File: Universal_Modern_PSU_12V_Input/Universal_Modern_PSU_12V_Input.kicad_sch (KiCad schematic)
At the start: 24 parts, among them J1 +12VDC Input, J2 Power Output, Q1 SUP53P06-20-E3, U1 DFR0831, U2 NKE1212SC, U3 R-78CK5.0-0.5

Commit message: Thickened +5V & +12V tracks
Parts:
- C2: footprint Capacitor_THT:C_Radial_D6.3mm_H7.0mm_P2.50mm -> Capacitor_THT:CP_Radial_D6.3mm_P2.50mm
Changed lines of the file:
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@@
 		)
 	)
-	(text_box "Power Input\nUse a well-regulated 4-5A +12VDC power supply.\nExpects centre-postive polarity.\nMOSFET Q1 will block in case centre-negative is used.\nIf not required, bridge pins 2 (drain) and 3 (source)."
+	(text_box "Power Input\nUse a well-regulated ≥5A +12VDC power supply.\nExpects centre-postive polarity.\nMOSFET Q1 will block in case centre-negative is used.\nIf not required, bridge pins 2 (drain) and 3 (source)."
 		(exclude_from_sim no)
 		(at 25.4 50.8 0)
@@
 			)
 		)
-		(property "Footprint" "Capacitor_THT:C_Radial_D6.3mm_H7.0mm_P2.50mm"
+		(property "Footprint" "Capacitor_THT:CP_Radial_D6.3mm_P2.50mm"
 			(at 176.53 99.3648 0)
 			(effects

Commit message: Additional vias for heat conduction
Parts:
- C2: value 10µF -> 100µF; footprint Capacitor_THT:CP_Radial_D6.3mm_P2.50mm -> Capacitor_THT:CP_Radial_D8.0mm_P5.00mm
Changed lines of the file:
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@@
 			)
 		)
-		(property "Value" "10µF"
+		(property "Value" "100µF"
 			(at 177.546 98.806 90)
 			(effects
@@
 			)
 		)
-		(property "Footprint" "Capacitor_THT:CP_Radial_D6.3mm_P2.50mm"
+		(property "Footprint" "Capacitor_THT:CP_Radial_D8.0mm_P5.00mm"
 			(at 176.53 99.3648 0)
 			(effects

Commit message: Minor PCB & schematic changes
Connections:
- net +12V_{OUT} is gone; now on net +12V_{IN}: C2.1, C3.1, C6.1, C7.2, D1.2 (A), J2.2 (Pin_2), Q1.3 (S), TP2.1, U1.2 (IN+), U2.2 (+VIN), U3.1 (+VIN)
- net +12V_{IN}: no longer J1.1, Q1.2 (D)
- new net +12V_{SUPPLY}: J1.1, Q1.2 (D)
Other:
- moved on the sheet: H1, H2, H3, H4, J2, TP1

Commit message: Further refinements to PCB layout
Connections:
- net +5V_{OUT}: now also J2.5 (Pin_5); no longer J2.3 (Pin_3)
- net -5V_{OUT}: now also J2.3 (Pin_3); no longer J2.5 (Pin_5)

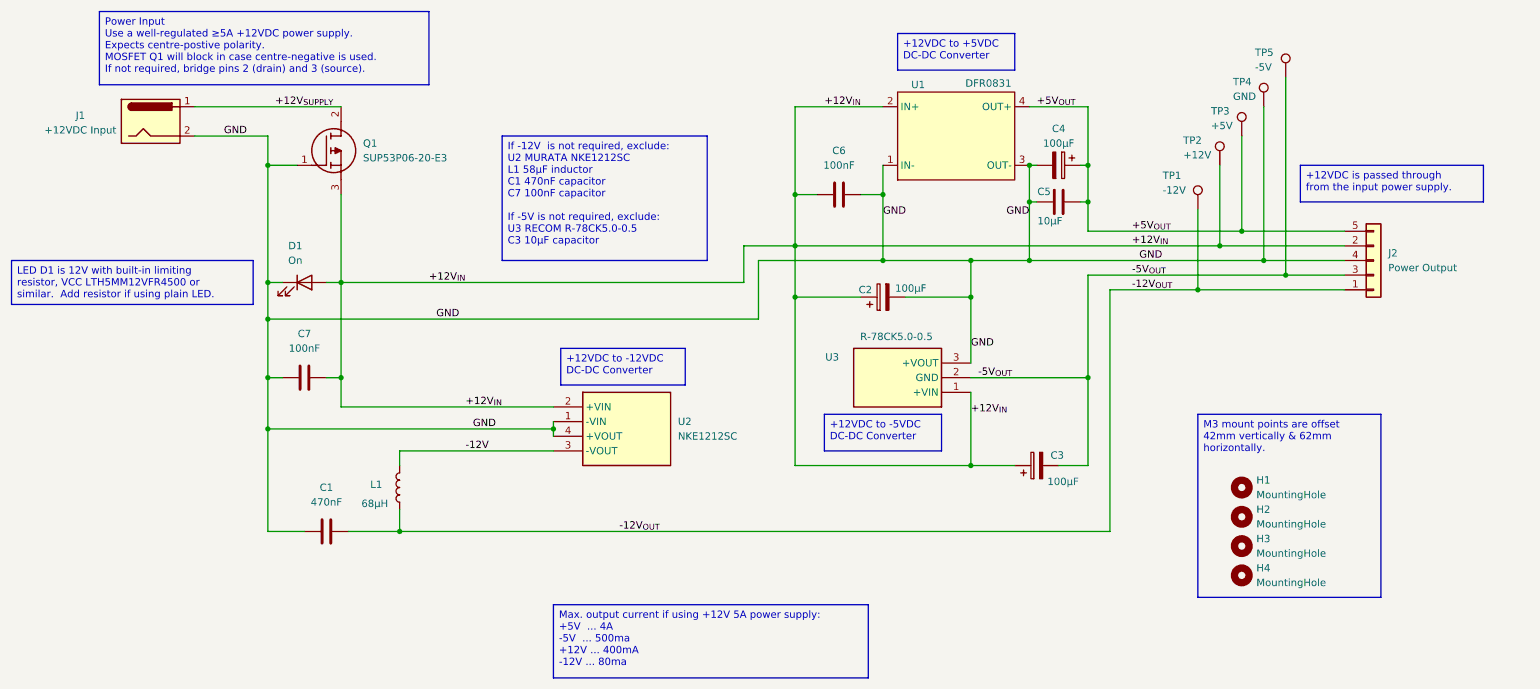
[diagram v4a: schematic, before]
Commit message: Add PS_ON soft-on pin
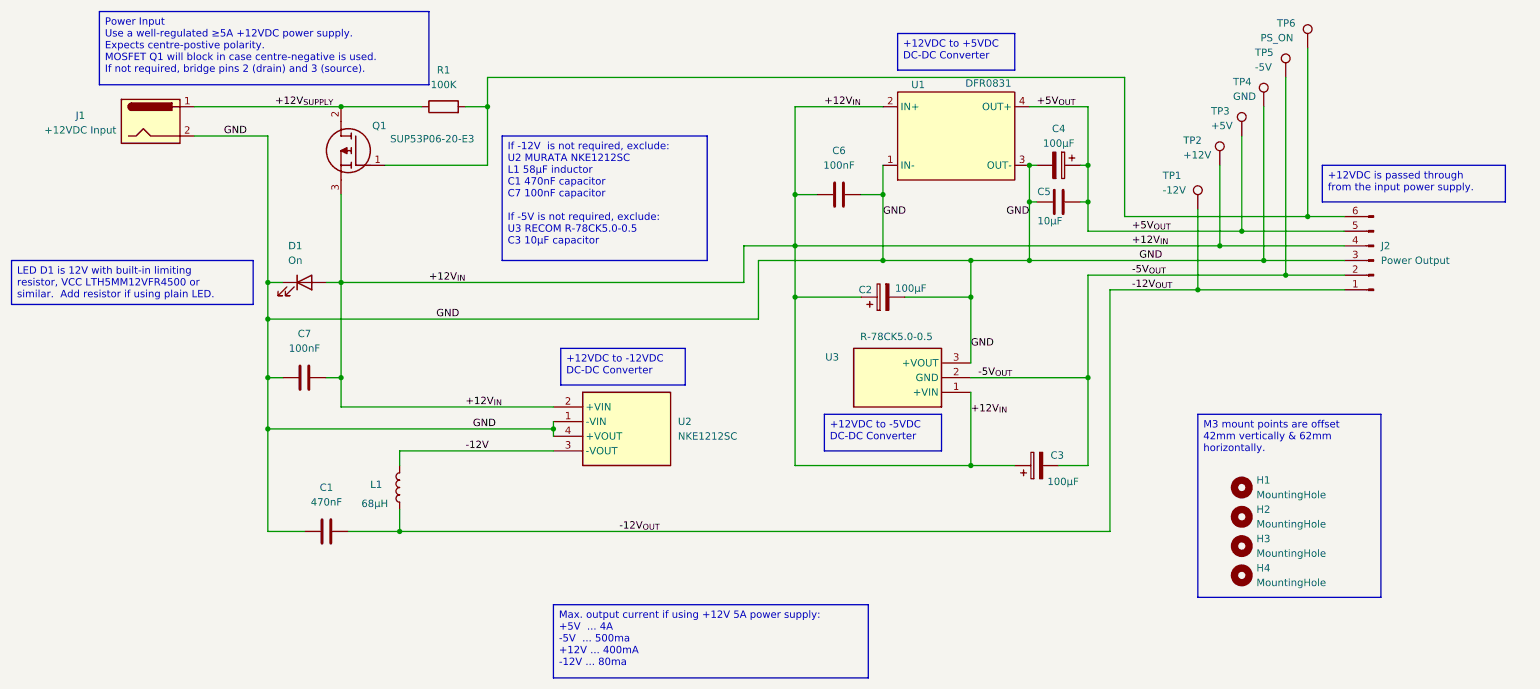
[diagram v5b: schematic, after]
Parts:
- added R1: 100K, symbol Device:R
- added TP6: PS_ON, TestPoint:TestPoint_Pad_D2.5mm, symbol Connector:TestPoint
- J2: symbol Connector_Generic:Conn_01x05 -> Connector:Conn_01x06_Pin
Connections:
- net +12V_{IN}: now also J2.4 (Pin_4); no longer J2.2 (Pin_2)
- net +12V_{SUPPLY}: now also R1.1
- net -5V_{OUT}: now also J2.2 (Pin_2); no longer J2.3 (Pin_3)
- net GND: now also J2.3 (Pin_3); no longer J2.4 (Pin_4), Q1.1 (G)
- new net: J2.6 (Pin_6), Q1.1 (G), R1.2, TP6.1
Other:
- moved on the sheet: Q1

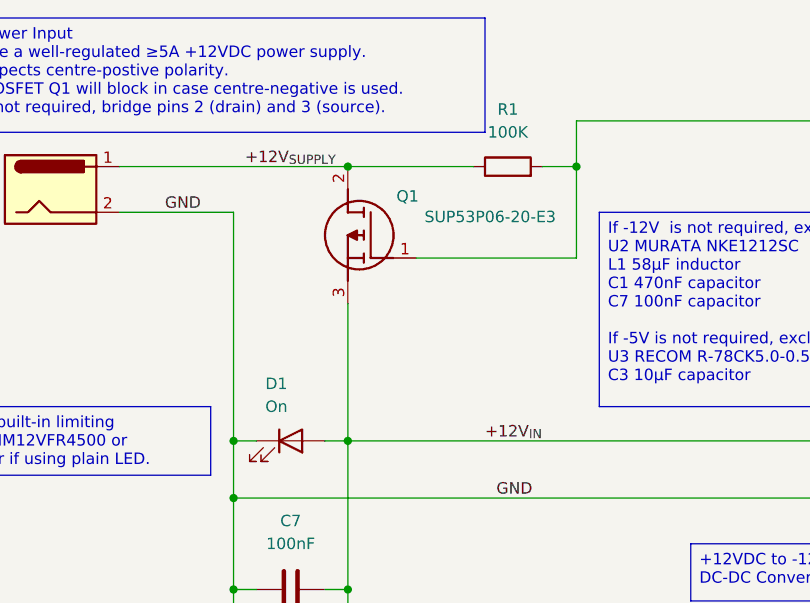
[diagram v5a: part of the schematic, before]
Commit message: Add original Q1 back.
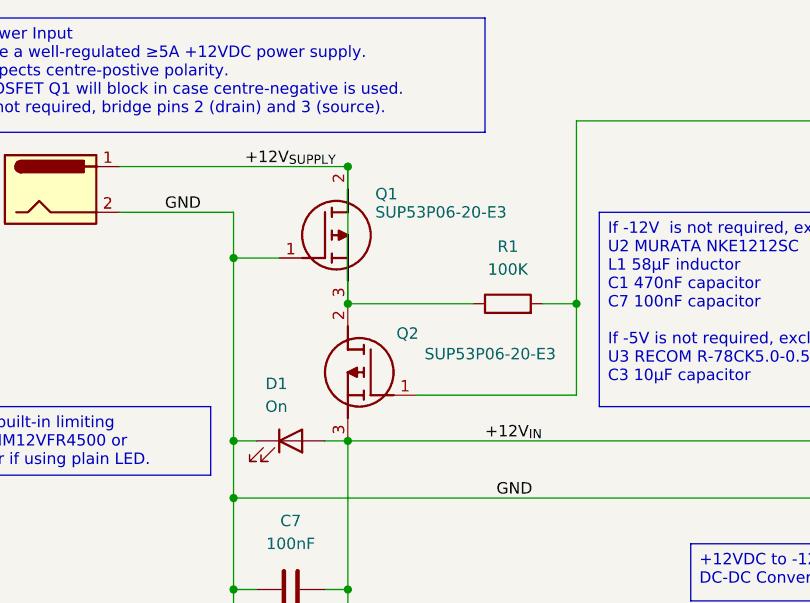
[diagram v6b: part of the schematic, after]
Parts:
- added Q1: SUP53P06-20-E3, Clueless_Engineer:TO254P465X1028X1931-3P, symbol Clueless_Engineer:SUP53P06-20-E3
- renumbered Q1 to Q2
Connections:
- net +12V_{SUPPLY}: now also Q1.2 (D), Q1.3 (S)
- net GND: now also Q1.1 (G)
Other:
- moved on the sheet: Q2, R1
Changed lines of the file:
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@@
 	)
 	(junction
+		(at 66.04 77.47)
+		(diameter 0)
+		(color 0 0 0 0)
+	)
+	(junction
 		(at 187.96 93.98)
 		(diameter 0)
@@
 	)
 	(junction
+		(at 78.74 82.55)
+		(diameter 0)
+		(color 0 0 0 0)
+	)
+	(junction
 		(at 187.96 100.33)
 		(diameter 0)
@@
 	)
 	(junction
+		(at 104.14 82.55)
+		(diameter 0)
+		(color 0 0 0 0)
+	)
+	(junction
 		(at 78.74 97.79)
 		(diameter 0)
@@
 	)
 	(junction
-		(at 104.14 67.31)
-		(diameter 0)
-		(color 0 0 0 0)
-	)
-	(junction
 		(at 172.72 82.55)
 		(diameter 0)
@@
 	(wire
 		(pts
-			(xy 104.14 67.31) (xy 104.14 62.23)
-		)
-		(stroke
-			(width 0)
-			(type default)
-		)
-	)
-	(wire
-		(pts
 			(xy 198.12 77.47) (xy 198.12 83.82)
 		)
@@
 	(wire
 		(pts
-			(xy 207.01 77.47) (xy 208.28 77.47)
+			(xy 66.04 77.47) (xy 71.12 77.47)
 		)
 		(stroke
@@
 	(wire
 		(pts
-			(xy 238.76 67.31) (xy 238.76 93.98)
+			(xy 207.01 77.47) (xy 208.28 77.47)
 		)
 		(stroke
@@
 	(wire
 		(pts
-			(xy 78.74 82.55) (xy 78.74 97.79)
+			(xy 238.76 67.31) (xy 238.76 93.98)
 		)
 		(stroke
@@
 	(wire
 		(pts
+			(xy 104.14 62.23) (xy 104.14 82.55)
+		)
+		(stroke
+			(width 0)
+			(type default)
+		)
+	)
+	(wire
+		(pts
 			(xy 115.57 123.19) (xy 115.57 124.46)
 		)
@@
 	(wire
 		(pts
+			(xy 66.04 77.47) (xy 66.04 97.79)
+		)
+		(stroke
+			(width 0)
+			(type default)
+		)
+	)
+	(wire
+		(pts
 			(xy 198.12 83.82) (xy 198.12 93.98)
 		)
@@
 	(wire
 		(pts
-			(xy 86.36 77.47) (xy 104.14 77.47)
+			(xy 86.36 92.71) (xy 104.14 92.71)
 		)
 		(stroke
@@
 	(wire
 		(pts
-			(xy 78.74 67.31) (xy 92.71 67.31)
+			(xy 78.74 82.55) (xy 92.71 82.55)
 		)
 		(stroke
@@
 	(wire
 		(pts
-			(xy 104.14 77.47) (xy 104.14 67.31)
+			(xy 104.14 92.71) (xy 104.14 82.55)
 		)
 		(stroke
@@
 	(wire
 		(pts
-			(xy 100.33 67.31) (xy 104.14 67.31)
+			(xy 100.33 82.55) (xy 104.14 82.55)
 		)
 		(stroke
@@
 	(wire
 		(pts
+			(xy 78.74 82.55) (xy 78.74 67.31)
+		)
+		(stroke
+			(width 0)
+			(type default)
+		)
+	)
+	(wire
+		(pts
 			(xy 208.28 77.47) (xy 208.28 67.31)
 		)
@@
 	(wire
 		(pts
-			(xy 66.04 72.39) (xy 66.04 97.79)
+			(xy 66.04 72.39) (xy 66.04 77.47)
 		)
 		(stroke
@@
 	(symbol
 		(lib_id "Clueless_Engineer:SUP53P06-20-E3")
-		(at 86.36 77.47 0)
+		(at 86.36 92.71 0)
 		(mirror y)
 		(unit 1)
@@
 		(in_pos_files yes)
 		(dnp no)
-		(property "Reference" "Q1"
-			(at 86.614 70.612 0)
+		(property "Reference" "Q2"
+			(at 86.614 85.852 0)
 			(show_name no)
 			(do_not_autoplace no)
@@
 		)
 		(property "Value" "SUP53P06-20-E3"
-			(at 101.854 72.898 0)
+			(at 101.854 88.138 0)
 			(show_name no)
 			(do_not_autoplace no)
@@
 		)
 		(property "Footprint" "Clueless_Engineer:TO254P465X1028X1931-3P"
-			(at 74.93 176.2 0)
+			(at 74.93 191.44 0)
 			(hide yes)
 			(show_name no)
@@
 		)
 		(property "Datasheet" "https://datasheet.datasheetarchive.com/originals/distributors/Datasheets-DGA24/1593239.pdf"
-			(at 74.93 276.2 0)
+			(at 74.93 291.44 0)
 			(hide yes)
 			(show_name no)
@@
 		)
 		(property "Description" "VISHAY - SUP53P06-20-E3 - MOSFET, P, TO-220"
-			(at 86.36 77.47 0)
+			(at 86.36 92.71 0)
 			(hide yes)
 			(show_name no)
@@
 		)
 		(property "Height" "4.65"
-			(at 74.93 476.2 0)
+			(at 74.93 491.44 0)
 			(hide yes)
 			(show_name no)
@@
 		)
 		(property "Mouser Part Number" "781-SUP53P06-20-E3"
-			(at 74.93 576.2 0)
+			(at 74.93 591.44 0)
 			(hide yes)
 			(show_name no)
@@
 		)
 		(property "Mouser Price/Stock" "https://www.mouser.co.uk/ProductDetail/Vishay-Semiconductors/SUP53P06-20-E3?qs=ru2xu5lizsADXHLEpSNjJA%3D%3D"
-			(at 74.93 676.2 0)
+			(at 74.93 691.44 0)
 			(hide yes)
 			(show_name no)
@@
 		)
 		(property "Manufacturer_Name" "Vishay"
-			(at 74.93 776.2 0)
+			(at 74.93 791.44 0)
 			(hide yes)
 			(show_name no)
@@
 		)
 		(property "Manufacturer_Part_Number" "SUP53P06-20-E3"
-			(at 74.93 876.2 0)
+			(at 74.93 891.44 0)
 			(hide yes)
 			(show_name no)
@@
 			(project "Universal_Modern_PSU_12V_Input"
 				(path "/2243e882-c373-463b-80e4-1df760d60a2a"
-					(reference "Q1")
+					(reference "Q2")
 					(unit 1)
 				)
@@
 	)
 	(symbol
+		(lib_id "Clueless_Engineer:SUP53P06-20-E3")
+		(at 71.12 77.47 0)
+		(unit 1)
+		(body_style 1)
+		(exclude_from_sim no)
+		(in_bom yes)
+		(on_board yes)
+		(in_pos_files yes)
+		(dnp no)
+		(property "Reference" "Q1"
+			(at 81.788 70.358 0)
+			(show_name no)
+			(do_not_autoplace no)
+			(effects
+				(font
+					(size 1.27 1.27)
+				)
+				(justify left)
+			)
+		)
+		(property "Value" "SUP53P06-20-E3"
+			(at 81.788 72.39 0)
+			(show_name no)
+			(do_not_autoplace no)
+			(effects
+				(font
+					(size 1.27 1.27)
+				)
+				(justify left)
+			)
+		)
+		(property "Footprint" "Clueless_Engineer:TO254P465X1028X1931-3P"
+			(at 82.55 176.2 0)
+			(hide yes)
+			(show_name no)
+			(do_not_autoplace no)
+			(effects
+				(font
+					(size 1.27 1.27)
+				)
+				(justify left top)
+			)
+		)
+		(property "Datasheet" "https://datasheet.datasheetarchive.com/originals/distributors/Datasheets-DGA24/1593239.pdf"
+			(at 82.55 276.2 0)
+			(hide yes)
+			(show_name no)
+			(do_not_autoplace no)
+			(effects
+				(font
+					(size 1.27 1.27)
+				)
+				(justify left top)
+			)
+		)
+		(property "Description" "VISHAY - SUP53P06-20-E3 - MOSFET, P, TO-220"
+			(at 71.12 77.47 0)
+			(hide yes)
+			(show_name no)
+			(do_not_autoplace no)
+			(effects
+				(font
+					(size 1.27 1.27)
+				)
+			)
+		)
+		(property "Height" "4.65"
+			(at 82.55 476.2 0)
+			(hide yes)
+			(show_name no)
+			(do_not_autoplace no)
+			(effects
+				(font
+					(size 1.27 1.27)
+				)
+				(justify left top)
+			)
+		)
+		(property "Mouser Part Number" "781-SUP53P06-20-E3"
+			(at 82.55 576.2 0)
+			(hide yes)
+			(show_name no)
+			(do_not_autoplace no)
+			(effects
+				(font
+					(size 1.27 1.27)
+				)
+				(justify left top)
+			)
+		)
+		(property "Mouser Price/Stock" "https://www.mouser.co.uk/ProductDetail/Vishay-Semiconductors/SUP53P06-20-E3?qs=ru2xu5lizsADXHLEpSNjJA%3D%3D"
+			(at 82.55 676.2 0)
+			(hide yes)
+			(show_name no)
+			(do_not_autoplace no)
+			(effects
+				(font
+					(size 1.27 1.27)
+				)
+				(justify left top)
+			)
+		)
+		(property "Manufacturer_Name" "Vishay"
+			(at 82.55 776.2 0)
+			(hide yes)
+			(show_name no)
+			(do_not_autoplace no)
+			(effects
+				(font
+					(size 1.27 1.27)
+				)
+				(justify left top)
+			)
+		)
+		(property "Manufacturer_Part_Number" "SUP53P06-20-E3"
+			(at 82.55 876.2 0)
+			(hide yes)
+			(show_name no)
+			(do_not_autoplace no)
+			(effects
+				(font
+					(size 1.27 1.27)
+				)
+				(justify left top)
+			)
+		)
+		(pin "2"
+		)
+		(pin "3"
+		)
+		(pin "1"
+		)
+		(instances
+			(project "Universal_Modern_PSU_12V_Input"
+				(path "/2243e882-c373-463b-80e4-1df760d60a2a"
+					(reference "Q1")
+					(unit 1)
+				)
+			)
+		)
+	)
+	(symbol
 		(lib_id "Device:R")
-		(at 96.52 67.31 90)
+		(at 96.52 82.55 90)
 		(unit 1)
 		(body_style 1)
@@
 		(fields_autoplaced yes)
 		(property "Reference" "R1"
-			(at 96.52 60.96 90)
+			(at 96.52 76.2 90)
 			(show_name no)
 			(do_not_autoplace no)
@@
 		)
 		(property "Value" "100K"
-			(at 96.52 63.5 90)
+			(at 96.52 78.74 90)
 			(show_name no)
 			(do_not_autoplace no)
@@
 		)
 		(property "Footprint" ""
-			(at 96.52 69.088 90)
+			(at 96.52 84.328 90)
 			(hide yes)
 			(show_name no)
@@
 		)
 		(property "Datasheet" ""
-			(at 96.52 67.31 0)
+			(at 96.52 82.55 0)
 			(hide yes)
 			(show_name no)
@@
 		)
 		(property "Description" "Resistor"
-			(at 96.52 67.31 0)
+			(at 96.52 82.55 0)
 			(hide yes)
 			(show_name no)

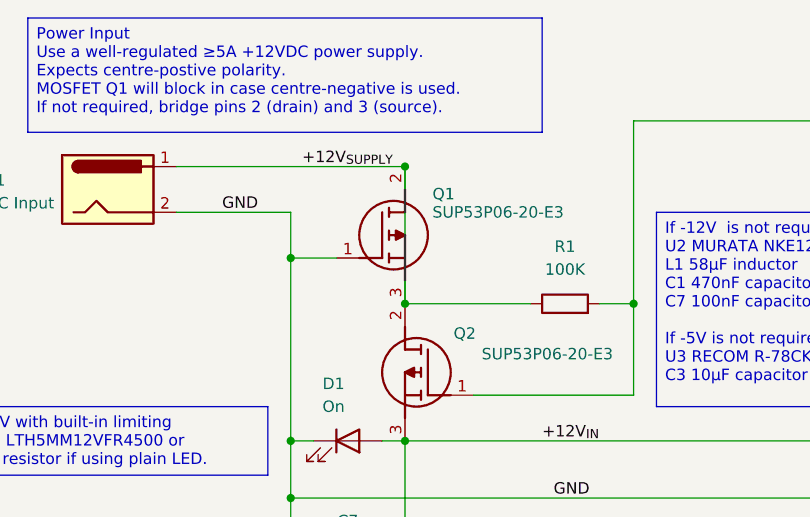
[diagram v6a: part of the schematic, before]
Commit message: Remove extra wire in Q1
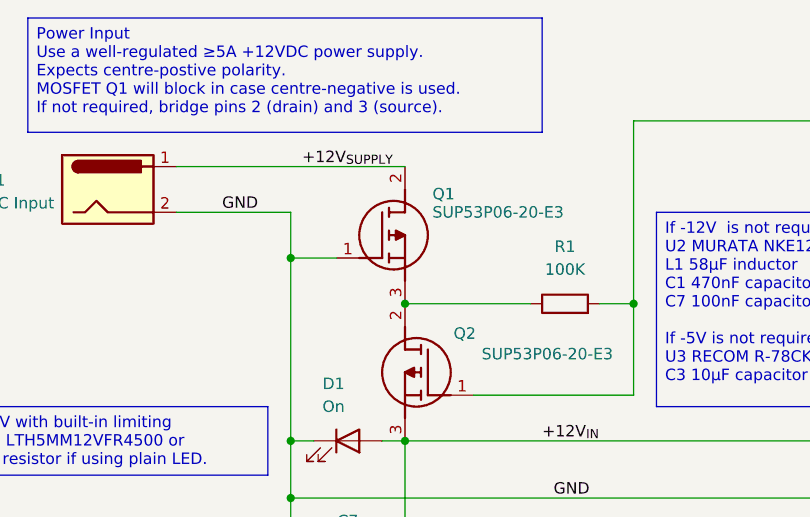
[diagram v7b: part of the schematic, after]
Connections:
- net +12V_{SUPPLY}: no longer Q1.3 (S), Q2.2 (D), R1.1
- new net: Q1.3 (S), Q2.2 (D), R1.1
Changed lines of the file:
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@@
-	)
-	(junction
-		(at 78.74 67.31)
-		(diameter 0)
-		(color 0 0 0 0)
 	)
 	(junction
@@
 		)
 		(stroke
-			(width 0)
-			(type default)
-		)
-	)
-	(wire
-		(pts
-			(xy 78.74 82.55) (xy 78.74 67.31)
-		)
-		(stroke
